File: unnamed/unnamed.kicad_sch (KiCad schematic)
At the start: 70 parts, among them J1 Serial, J2 Serial, SW1 SW_Push, SW10 SW_Push, SW11 SW_Push, SW12 SW_Push, SW13 SW_Push, SW14 SW_Push, SW15 SW_Push, SW16 SW_Push, SW17 SW_Push, SW18 SW_Push, SW19 SW_Push, SW2 SW_Push, SW20 SW_Push, SW21 SW_Push, SW22 SW_Push, SW23 SW_Push, SW24 SW_Push, SW25 SW_SPST, SW26 SW_SPST, SW3 SW_Push, SW4 SW_Push, SW5 SW_Push, SW6 SW_Push, SW7 SW_Push, SW8 SW_Push, SW9 SW_Push, U1 eliteC, U2 eliteC

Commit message: go back to 3x5
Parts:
- removed C1, C2: C, Capacitor_SMD:C_1206_3216Metric_Pad1.42x1.75mm_HandSolder, symbol Device:C
- removed D1, D13, D15, D2, D20, D22, D27, D28, D34, D35, D7, D8: D_Schottky_x2_KCom_AAK, customs:TSOT-23_HandSoldering, symbol Device:D_Schottky_x2_KCom_AAK
- removed D10, D11, D12, D14, D16, D17, D18, D19, D21, D23, D24, D25, D26, D29, D3, D30, D31, D32, D33, D36, D4, D5, D6, D9: SK6812MINI, libs2:YS-SK6812MINI-E_REVERSE, symbol LED:SK6812MINI
- removed R1, R2: R, Resistor_SMD:R_1206_3216Metric_Pad1.42x1.75mm_HandSolder, symbol Device:R
- removed SW1, SW10, SW11, SW12, SW13, SW14, SW15, SW16, SW17, SW18, SW19, SW2, SW20, SW21, SW22, SW23, SW24, SW3, SW4, SW5, SW6, SW7, SW8, SW9: SW_Push, custom:SW_MX_reversible, symbol Switch:SW_Push
- added C? (x2): C, Capacitor_SMD:C_1206_3216Metric_Pad1.42x1.75mm_HandSolder, symbol Device:C
- added D? (x15): D, custom:Diode_TH_SOD123, symbol Device:D
- added D? (x15): SK6812MINI, libs2:YS-SK6812MINI-E_REVERSE, symbol LED:SK6812MINI
- added R? (x2): R, Resistor_SMD:R_1206_3216Metric_Pad1.42x1.75mm_HandSolder, symbol Device:R
- added SW? (x15): SW_Push, custom:SW_MX_reversible, symbol Switch:SW_Push
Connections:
- net Din: now also R?.1, R?.1
- net Dout: now also D?.1 (DOUT)
- net Gnd: now also C?.2, C?.2, D?.2 (VSS), D?.2 (VSS), D?.2 (VSS), D?.2 (VSS), D?.2 (VSS), D?.2 (VSS), D?.2 (VSS), D?.2 (VSS), D?.2 (VSS), D?.2 (VSS), D?.2 (VSS), D?.2 (VSS), D?.2 (VSS), D?.2 (VSS), D?.2 (VSS)
- net Vcc: now also C?.1, C?.1, D?.4 (VDD), D?.4 (VDD), D?.4 (VDD), D?.4 (VDD), D?.4 (VDD), D?.4 (VDD), D?.4 (VDD), D?.4 (VDD), D?.4 (VDD), D?.4 (VDD), D?.4 (VDD), D?.4 (VDD), D?.4 (VDD), D?.4 (VDD), D?.4 (VDD)
- net col2: now also D?.1 (K), D?.1 (K), D?.1 (K)
- net col3: now also D?.1 (K), D?.1 (K), D?.1 (K)
- net col4: now also D?.1 (K), D?.1 (K), D?.1 (K)
- net col5: now also D?.1 (K), D?.1 (K), D?.1 (K)
- net col6: now also D?.1 (K), D?.1 (K), D?.1 (K)
- net row2: now also SW?.1, SW?.1, SW?.1, SW?.1, SW?.1
- net row3: now also SW?.1, SW?.1, SW?.1, SW?.1, SW?.1
- net row4: now also SW?.1, SW?.1, SW?.1, SW?.1, SW?.1
- new net: D?.2 (A), SW?.2 (x15)
- new net: D?.1 (DOUT), D?.3 (DIN) (x14)
- new net: D?.3 (DIN), R?.2, R?.2

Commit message: rgb left and right
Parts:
- removed C?: C, Capacitor_SMD:C_1206_3216Metric_Pad1.42x1.75mm_HandSolder, symbol Device:C
- removed R?: R, Resistor_SMD:R_1206_3216Metric_Pad1.42x1.75mm_HandSolder, symbol Device:R
- added C2: C, Capacitor_SMD:C_1206_3216Metric_Pad1.42x1.75mm_HandSolder, symbol Device:C
- added D30, D33, D37, D38, D39, D42, D43, D44, D47, D48, D49, D52, D53, D54, D58, D59, D60, D64, D67: D, custom:Diode_TH_SOD123, symbol Device:D
- added D31, D34, D35, D36, D40, D41, D45, D46, D50, D51, D55, D56, D57, D61, D62, D63, D65, D66, D68: SK6812MINI, libs2:YS-SK6812MINI-E_REVERSE, symbol LED:SK6812MINI
- added R2: R, Resistor_SMD:R_1206_3216Metric_Pad1.42x1.75mm_HandSolder, symbol Device:R
- added SW16, SW17, SW18, SW19, SW20, SW21, SW22, SW23, SW24, SW27, SW28, SW29, SW30, SW31, SW32, SW33, SW34, SW35, SW36: SW_Push, custom:SW_MX_reversible, symbol Switch:SW_Push
- gave numbers to parts that had none: 47
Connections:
- net Din is gone; now on net rgb_l: R1.1
- net Gnd is gone; now on net GND: C1.2, D1.2 (VSS), D11.2 (VSS), D12.2 (VSS), D16.2 (VSS), D17.2 (VSS), D2.2 (VSS), D21.2 (VSS), D22.2 (VSS), D23.2 (VSS), D27.2 (VSS), D28.2 (VSS), D29.2 (VSS), D32.2 (VSS), D6.2 (VSS), D7.2 (VSS)
- net Vcc is gone; now on net +5V: C1.1, D1.4 (VDD), D11.4 (VDD), D12.4 (VDD), D16.4 (VDD), D17.4 (VDD), D2.4 (VDD), D21.4 (VDD), D22.4 (VDD), D23.4 (VDD), D27.4 (VDD), D28.4 (VDD), D29.4 (VDD), D32.4 (VDD), D6.4 (VDD), D7.4 (VDD)
- net col2 is gone; now on net col2_l: D3.1 (K), D4.1 (K), D5.1 (K)
- net col3 is gone; now on net col3_l: D10.1 (K), D8.1 (K), D9.1 (K)
- net col4 is gone; now on net col4_l: D13.1 (K), D14.1 (K), D15.1 (K)
- net col5 is gone; now on net col5_l: D18.1 (K), D19.1 (K), D20.1 (K)
- net col6 is gone; now on net col6_l: D24.1 (K), D25.1 (K), D26.1 (K)
- net row2 is gone; now on net row2_l: SW1.1, SW10.1, SW13.1, SW4.1, SW7.1
- net row3 is gone; now on net row3_l: SW11.1, SW14.1, SW2.1, SW5.1, SW8.1
- net row4 is gone; now on net row4_l: SW12.1, SW15.1, SW3.1, SW6.1, SW9.1
- net +5V: now also C2.1, D31.4 (VDD), D34.4 (VDD), D35.4 (VDD), D36.4 (VDD), D40.4 (VDD), D41.4 (VDD), D45.4 (VDD), D46.4 (VDD), D50.4 (VDD), D51.4 (VDD), D55.4 (VDD), D56.4 (VDD), D57.4 (VDD), D61.4 (VDD), D62.4 (VDD), D63.4 (VDD), D65.4 (VDD), D66.4 (VDD), D68.4 (VDD)
- net Dout: now also D34.1 (DOUT), D68.1 (DOUT); no longer D28.1 (DOUT)
- net GND: now also C2.2, D31.2 (VSS), D34.2 (VSS), D35.2 (VSS), D36.2 (VSS), D40.2 (VSS), D41.2 (VSS), D45.2 (VSS), D46.2 (VSS), D50.2 (VSS), D51.2 (VSS), D55.2 (VSS), D56.2 (VSS), D57.2 (VSS), D61.2 (VSS), D62.2 (VSS), D63.2 (VSS), D65.2 (VSS), D66.2 (VSS), D68.2 (VSS); no longer SW25.2 (B)
- net col2_l: now also D30.1 (K)
- net col2_r: now also D37.1 (K), D38.1 (K), D39.1 (K), D64.1 (K)
- net col3_r: now also D42.1 (K), D43.1 (K), D44.1 (K)
- net col4_l: now also D33.1 (K)
- net col4_r: now also D47.1 (K), D48.1 (K), D49.1 (K), D67.1 (K)
- net col5_r: now also D52.1 (K), D53.1 (K), D54.1 (K)
- net col6_r: now also D58.1 (K), D59.1 (K), D60.1 (K)
- net rgb_l: now also U2.1 (TX); no longer U1.1 (TX)
- net rgb_r: now also U1.1 (TX), R2.1; no longer U2.1 (TX)
- net row1_l: now also SW16.1, SW17.1
- net row1_r: now also SW35.1, SW36.1
- net row2_r: now also SW18.1, SW21.1, SW24.1, SW29.1, SW32.1
- net row3_r: now also SW19.1, SW22.1, SW27.1, SW30.1, SW33.1
- net row4_r: now also SW20.1, SW23.1, SW28.1, SW31.1, SW34.1
- net Rst renamed Rst_l
- net Rst2 renamed Rst_r
- net split_hand_l: no longer names the net of U2.28 (F1)
- net split_hand_r: no longer names the net of U1.28 (F1)
- new net: D31.1 (DOUT), D34.3 (DIN)
- new net: D59.2 (A), SW33.2
- new net: D60.2 (A), SW34.2
- new net: D46.1 (DOUT), D51.3 (DIN)
- new net: D40.1 (DOUT), D46.3 (DIN)
- new net: D42.2 (A), SW21.2
- new net: D51.1 (DOUT), D56.3 (DIN)
- new net: D38.2 (A), SW19.2
- new net: D56.1 (DOUT), D61.3 (DIN)
- new net: D62.1 (DOUT), D65.3 (DIN)
- new net: D57.1 (DOUT), D62.3 (DIN)
- new net: D45.1 (DOUT), D50.3 (DIN)
- new net: D41.1 (DOUT), D45.3 (DIN)
- new net: D47.2 (A), SW24.2
- new net: D64.2 (A), SW35.2
- new net: D53.2 (A), SW30.2
- new net: D55.1 (DOUT), D57.3 (DIN)
- new net: D50.1 (DOUT), D55.3 (DIN)
- new net: D28.1 (DOUT), D31.3 (DIN)
- new net: D30.2 (A), SW16.2
- new net: D67.2 (A), SW36.2
- new net: D37.2 (A), SW18.2
- new net: D39.2 (A), SW20.2
- new net: D63.1 (DOUT), D66.3 (DIN)
- new net: D61.1 (DOUT), D63.3 (DIN)
- new net: D36.3 (DIN), D66.1 (DOUT)
- new net: D58.2 (A), SW32.2
- new net: D49.2 (A), SW28.2
- new net: D54.2 (A), SW31.2
- new net: D36.1 (DOUT), D41.3 (DIN)
- new net: D65.1 (DOUT), D68.3 (DIN)
- new net: D48.2 (A), SW27.2
- new net: D35.3 (DIN), R2.2
- new net: D52.2 (A), SW29.2
- new net: D35.1 (DOUT), D40.3 (DIN)
- new net: D33.2 (A), SW17.2
- new net: D43.2 (A), SW22.2
- new net: D44.2 (A), SW23.2
- no-connect marks 8 -> 10
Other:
- note added: "Diodes and switches - plate"
- note added: "Diodes and switches - thumb cluster"
- note added: "Left"
- note added: "RGB - plate and thumb cluster"
- note added: "Right"
- note removed: "Diodes and switches"
- note removed: "RGB"
- moved on the sheet: C1, D1, D11, D12, D16, D17, D2, D21, D22, D23, D27, D28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

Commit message: erc
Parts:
- added J3, J4: Conn_01x01_Female, symbol Connector:Conn_01x01_Female
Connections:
- net +5V: no longer C1.1, D1.4 (VDD), D11.4 (VDD), D12.4 (VDD), D16.4 (VDD), D17.4 (VDD), D2.4 (VDD), D21.4 (VDD), D22.4 (VDD), D23.4 (VDD), D27.4 (VDD), D28.4 (VDD), D29.4 (VDD), D31.4 (VDD), D32.4 (VDD), D34.4 (VDD), D6.4 (VDD), D7.4 (VDD), J2.T, U1.21 (VCC), U2.21 (VCC)
- net GND: now also SW25.2 (B); no longer C1.2, D1.2 (VSS), D11.2 (VSS), D12.2 (VSS), D16.2 (VSS), D17.2 (VSS), D2.2 (VSS), D21.2 (VSS), D22.2 (VSS), D23.2 (VSS), D27.2 (VSS), D28.2 (VSS), D29.2 (VSS), D31.2 (VSS), D32.2 (VSS), D34.2 (VSS), D6.2 (VSS), D7.2 (VSS), J2.R1, SW26.2 (B), U1.23 (GND), U1.3 (GND), U1.4 (GND), U2.23 (GND), U2.3 (GND), U2.4 (GND)
- net Dout renamed Dout_l
- net Dout_l: now also J4.1 (Pin_1); no longer D68.1 (DOUT)
- new net +5VL: C1.1, D1.4 (VDD), D11.4 (VDD), D12.4 (VDD), D16.4 (VDD), D17.4 (VDD), D2.4 (VDD), D21.4 (VDD), D22.4 (VDD), D23.4 (VDD), D27.4 (VDD), D28.4 (VDD), D29.4 (VDD), D31.4 (VDD), D32.4 (VDD), D34.4 (VDD), D6.4 (VDD), D7.4 (VDD), J2.T, U1.21 (VCC), U2.21 (VCC)
- new net Dout_r: D68.1 (DOUT), J3.1 (Pin_1)
- new net GND2: C1.2, D1.2 (VSS), D11.2 (VSS), D12.2 (VSS), D16.2 (VSS), D17.2 (VSS), D2.2 (VSS), D21.2 (VSS), D22.2 (VSS), D23.2 (VSS), D27.2 (VSS), D28.2 (VSS), D29.2 (VSS), D31.2 (VSS), D32.2 (VSS), D34.2 (VSS), D6.2 (VSS), D7.2 (VSS), J2.R1, SW26.2 (B), U1.23 (GND), U1.3 (GND), U1.4 (GND), U2.23 (GND), U2.3 (GND), U2.4 (GND)

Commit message: align stuff
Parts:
- C1, C2: footprint Capacitor_SMD:C_1206_3216Metric_Pad1.42x1.75mm_HandSolder -> (none)
- D1, D11, D12, D16, D17, D2, D21, D22, D23, D27, D28, D29, D31, D32, D34, D35, D36, D40, D41, D45, D46, D50, D51, D55, D56, D57, D6, D61, D62, D63, D65, D66, D68, D7: footprint libs2:YS-SK6812MINI-E_REVERSE -> (none)
- D10, D13, D14, D15, D18, D19, D20, D24, D25, D26, D3, D30, D33, D37, D38, D39, D4, D42, D43, D44, D47, D48, D49, D5, D52, D53, D54, D58, D59, D60, D64, D67, D8, D9: footprint custom:Diode_TH_SOD123 -> (none)
- J1, J2: footprint Library:Jack_3.5mm_PJ320E_Horizontal -> (none)
- R1, R2: footprint Resistor_SMD:R_1206_3216Metric_Pad1.42x1.75mm_HandSolder -> (none)
- SW1, SW10, SW11, SW12, SW13, SW14, SW15, SW16, SW17, SW18, SW19, SW2, SW20, SW21, SW22, SW23, SW24, SW27, SW28, SW29, SW3, SW30, SW31, SW32, SW33, SW4, SW5, SW6, SW7, SW8, SW9: footprint custom:SW_MX_reversible -> Library:SW_MX_choc
- SW25, SW26: footprint Library:PushSwitch -> Library:SW_MX_choc
- SW34, SW35, SW36: footprint custom:SW_MX_reversible -> (none)
- U1, U2: footprint Library:Elite-C -> (none)

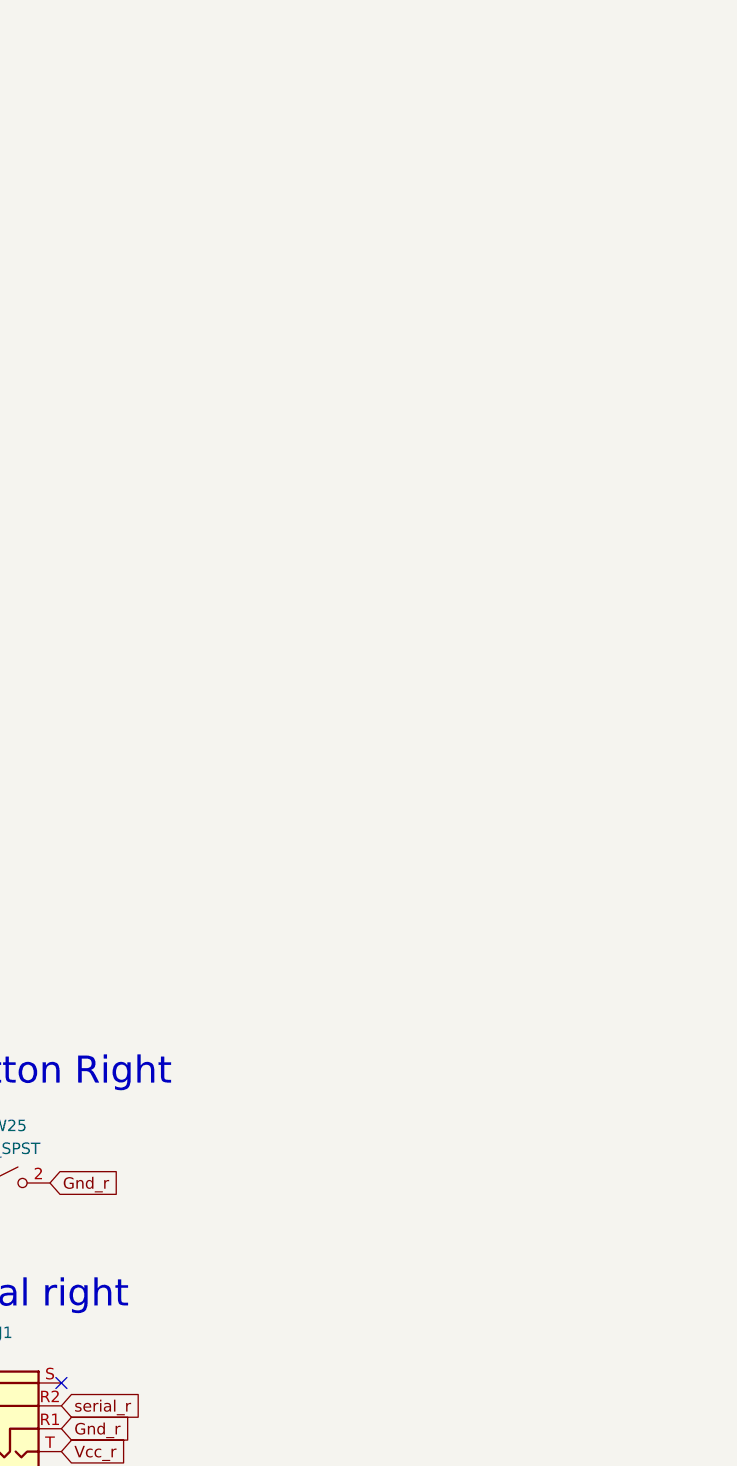
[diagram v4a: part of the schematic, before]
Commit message: Added 3 pin battery connector
3pin battery connector - idiot proofing to prevent burned MCUs
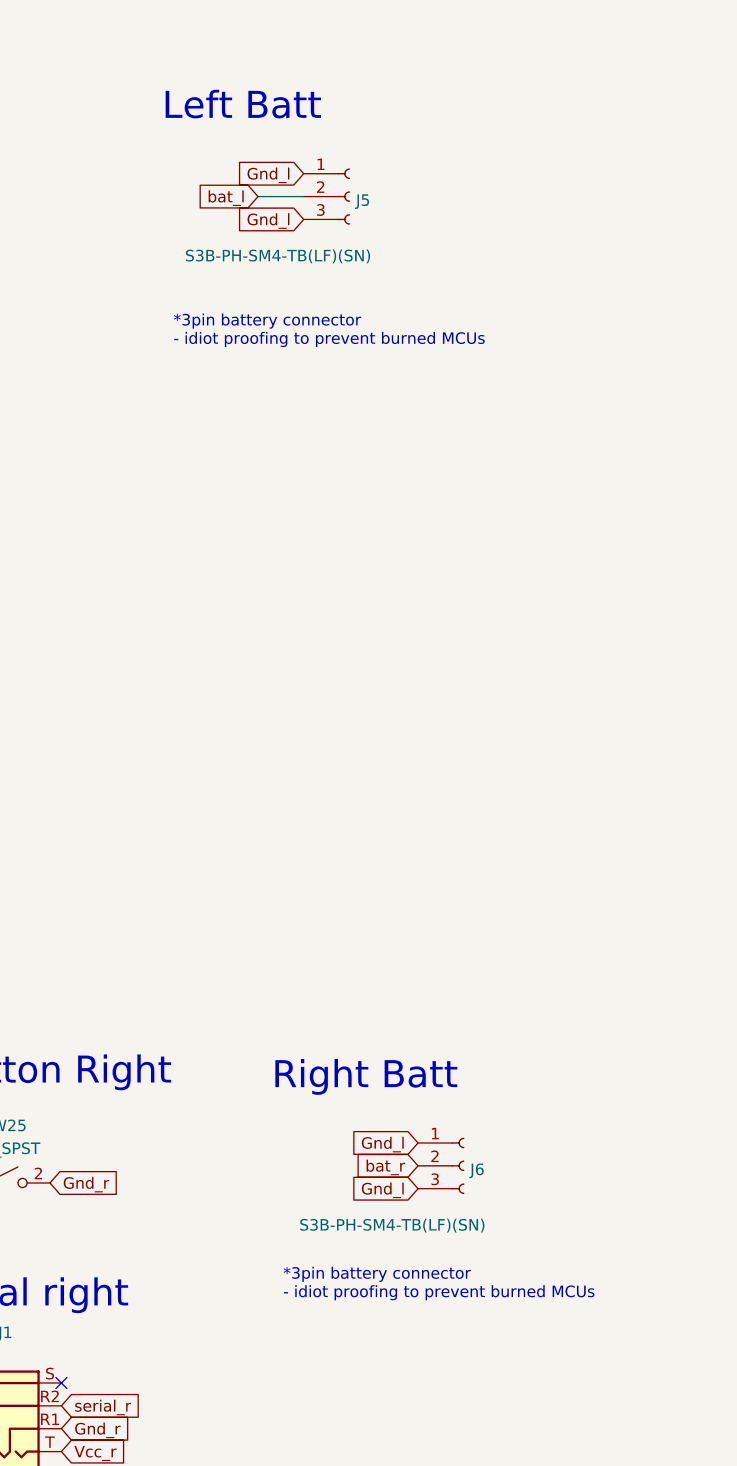
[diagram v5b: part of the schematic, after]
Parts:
- added J5, J6: S3B-PH-SM4-TB(LF)(SN), Connector_JST:JST_PH_S3B-PH-SM4-TB_1x03-1MP_P2.00mm_Horizontal, symbol Connector:Conn_01x03_Female
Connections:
- net GND2: now also J5.1 (Pin_1), J5.3 (Pin_3), J6.1 (Pin_1), J6.3 (Pin_3)
- net bat_l: now also J5.2 (Pin_2)
- net bat_r: now also J6.2 (Pin_2)
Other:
- note added: "*3pin battery connector - idiot proofing to prevent burned MCUs"
- note added: "Left Batt"
- note added: "Right Batt"
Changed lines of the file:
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@@
 (kicad_sch (version 20211123) (generator eeschema)
-  (paper "A3")
+  (paper "A1")
   (junction (at 114.3 71.12) (diameter 0) (color 0 0 0 0)
   )
@@
     (stroke (width 0) (type default) (color 0 0 0 0))
   )
+  (wire (pts (xy 421.894 35.814) (xy 426.974 35.814))
+    (stroke (width 0) (type default) (color 0 0 0 0))
+  )
   (wire (pts (xy 158.75 48.26) (xy 158.75 58.42))
     (stroke (width 0) (type default) (color 0 0 0 0))
@@
     (effects (font (size 3 3)) (justify left bottom))
   )
+  (text "Left Batt" (at 411.226 27.686 0)
+    (effects (font (size 3 3)) (justify left bottom))
+  )
   (text "Reset button Right" (at 373.634 134.874 0)
     (effects (font (size 3 3)) (justify left bottom))
@@
     (effects (font (size 3 3)) (justify left bottom))
   )
+  (text "Right Batt" (at 423.418 135.382 0)
+    (effects (font (size 3 3)) (justify left bottom))
+  )
   (text "MCU Right" (at 310.134 135.382 0)
     (effects (font (size 3 3)) (justify left bottom))
@@
     (effects (font (size 1.27 1.27)) (justify right bottom))
   )
+  (text "*3pin battery connector\n- idiot proofing to prevent burned MCUs"
+    (at 424.688 158.496 0)
+    (effects (font (size 1.27 1.27)) (justify left bottom))
+  )
   (text "Right" (at 22.86 167.005 90)
     (effects (font (size 5 5)) (justify left bottom))
@@
     (effects (font (size 1.27 1.27)) (justify right bottom))
   )
+  (text "*3pin battery connector\n- idiot proofing to prevent burned MCUs"
+    (at 412.496 52.578 0)
+    (effects (font (size 1.27 1.27)) (justify left bottom))
+  )
   (global_label "row2_r" (shape input) (at 44.45 135.255 180)
     (effects (font (size 1.27 1.27)) (justify right))
@@
     )
   )
+  (global_label "Gnd_l" (shape input) (at 426.974 38.354 180)
+    (effects (font (size 1.27 1.27)) (justify right))
+    (property "Intersheet References" "${INTERSHEET_REFS}" (id 0) (at 550.164 108.204 0)
+      (effects (font (size 1.27 1.27)) hide)
+    )
+  )
   (global_label "Gnd_l" (shape input) (at 303.53 156.21 180)
     (effects (font (size 1.27 1.27)) (justify right))
@@
     )
   )
+  (global_label "Gnd_l" (shape input) (at 426.974 33.274 180)
+    (effects (font (size 1.27 1.27)) (justify right))
+    (property "Intersheet References" "${INTERSHEET_REFS}" (id 0) (at 550.164 103.124 0)
+      (effects (font (size 1.27 1.27)) hide)
+    )
+  )
   (global_label "row1_l" (shape input) (at 318.77 45.72 0)
     (effects (font (size 1.27 1.27)) (justify left))
@@
     )
   )
+  (global_label "Gnd_l" (shape input) (at 439.674 146.05 180)
+    (effects (font (size 1.27 1.27)) (justify right))
+    (property "Intersheet References" "${INTERSHEET_REFS}" (id 0) (at 562.864 215.9 0)
+      (effects (font (size 1.27 1.27)) hide)
+    )
+  )
   (global_label "row4_l" (shape input) (at 283.21 50.8 180)
     (effects (font (size 1.27 1.27)) (justify right))
@@
     )
   )
+  (global_label "Gnd_l" (shape input) (at 439.674 140.97 180)
+    (effects (font (size 1.27 1.27)) (justify right))
+    (property "Intersheet References" "${INTERSHEET_REFS}" (id 0) (at 562.864 210.82 0)
+      (effects (font (size 1.27 1.27)) hide)
+    )
+  )
   (global_label "col2_r" (shape input) (at 339.09 161.29 0)
     (effects (font (size 1.27 1.27)) (justify left))
@@
     )
   )
+  (global_label "bat_l" (shape input) (at 421.894 35.814 180)
+    (effects (font (size 1.27 1.27)) (justify right))
+    (property "Intersheet References" "${INTERSHEET_REFS}" (id 0) (at 545.084 166.624 0)
+      (effects (font (size 1.27 1.27)) hide)
+    )
+  )
   (global_label "Gnd_l" (shape input) (at 50.8 86.36 180)
     (effects (font (size 1.27 1.27)) (justify right))
@@
     )
   )
+  (global_label "bat_r" (shape input) (at 439.674 143.51 180)
+    (effects (font (size 1.27 1.27)) (justify right))
+    (property "Intersheet References" "${INTERSHEET_REFS}" (id 0) (at 562.864 274.32 0)
+      (effects (font (size 1.27 1.27)) hide)
+    )
+  )
   (global_label "col3_r" (shape input) (at 105.41 132.715 90)
     (effects (font (size 1.27 1.27)) (justify left))
@@
     )
   )
+  (symbol (lib_id "Connector:Conn_01x03_Female") (at 432.054 35.814 0) (unit 1)
+    (in_bom yes) (on_board yes)
+    (property "Reference" "J5" (id 0) (at 432.7652 36.2493 0)
+      (effects (font (size 1.27 1.27)) (justify left))
+    )
+    (property "Value" "S3B-PH-SM4-TB(LF)(SN)" (id 1) (at 413.766 42.418 0)
+      (effects (font (size 1.27 1.27)) (justify left))
+    )
+    (property "Footprint" "Connector_JST:JST_PH_S3B-PH-SM4-TB_1x03-1MP_P2.00mm_Horizontal" (id 2) (at 432.054 35.814 0)
+      (effects (font (size 1.27 1.27)) hide)
+    )
+    (property "Datasheet" "~" (id 3) (at 432.054 35.814 0)
+      (effects (font (size 1.27 1.27)) hide)
+    )
+    (property "LCSC" "C265101" (id 4) (at 432.054 35.814 0)
+      (effects (font (size 1.27 1.27)) hide)
+    )
+    (pin "1")
+    (pin "2")
+    (pin "3")
+  )
   (symbol (lib_id "Device:D") (at 177.8 48.26 180) (unit 1)
     (in_bom yes) (on_board yes)
@@
     (pin "T")
   )
+  (symbol (lib_id "Connector:Conn_01x03_Female") (at 444.754 143.51 0) (unit 1)
+    (in_bom yes) (on_board yes)
+    (property "Reference" "J6" (id 0) (at 445.4652 143.9453 0)
+      (effects (font (size 1.27 1.27)) (justify left))
+    )
+    (property "Value" "S3B-PH-SM4-TB(LF)(SN)" (id 1) (at 426.466 150.114 0)
+      (effects (font (size 1.27 1.27)) (justify left))
+    )
+    (property "Footprint" "Connector_JST:JST_PH_S3B-PH-SM4-TB_1x03-1MP_P2.00mm_Horizontal" (id 2) (at 444.754 143.51 0)
+      (effects (font (size 1.27 1.27)) hide)
+    )
+    (property "Datasheet" "~" (id 3) (at 444.754 143.51 0)
+      (effects (font (size 1.27 1.27)) hide)
+    )
+    (property "LCSC" "C265101" (id 4) (at 444.754 143.51 0)
+      (effects (font (size 1.27 1.27)) hide)
+    )
+    (pin "1")
+    (pin "2")
+    (pin "3")
+  )
   (symbol (lib_id "Device:D") (at 151.13 48.26 180) (unit 1)
     (in_bom yes) (on_board yes)
@@
       (reference "J4") (unit 1) (value "Conn_01x01_Female") (footprint "")
     )
+    (path "/0024d4dc-bd5d-4def-a2be-39a78e329b8f"
+      (reference "J5") (unit 1) (value "S3B-PH-SM4-TB(LF)(SN)") (footprint "Connector_JST:JST_PH_S3B-PH-SM4-TB_1x03-1MP_P2.00mm_Horizontal")
+    )
+    (path "/dcaa4574-925b-47c6-8a27-5fe0c28d002f"
+      (reference "J6") (unit 1) (value "S3B-PH-SM4-TB(LF)(SN)") (footprint "Connector_JST:JST_PH_S3B-PH-SM4-TB_1x03-1MP_P2.00mm_Horizontal")
+    )
     (path "/74b3aa64-9363-448b-93d6-0b22421aa5c3"
